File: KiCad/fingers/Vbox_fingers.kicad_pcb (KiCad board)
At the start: 2 copper layers, 109 x 45 mm, 20 parts, among them J1 Conn_01x10, J2 Conn_01x10, SW1 SW_Push_45deg, SW10 SW_Push_45deg, SW11 SW_Push_45deg, SW12 SW_Push_45deg, SW13 SW_Push_45deg, SW14 SW_Push_45deg, SW15 SW_Push_45deg, SW16 SW_Push_45deg, SW17 SW_Push_45deg, SW18 SW_Push_45deg, SW2 SW_Push_45deg, SW3 SW_Push_45deg, SW4 SW_Push_45deg, SW5 SW_Push_45deg, SW6 SW_Push_45deg, SW7 SW_Push_45deg, SW8 SW_Push_45deg, SW9 SW_Push_45deg

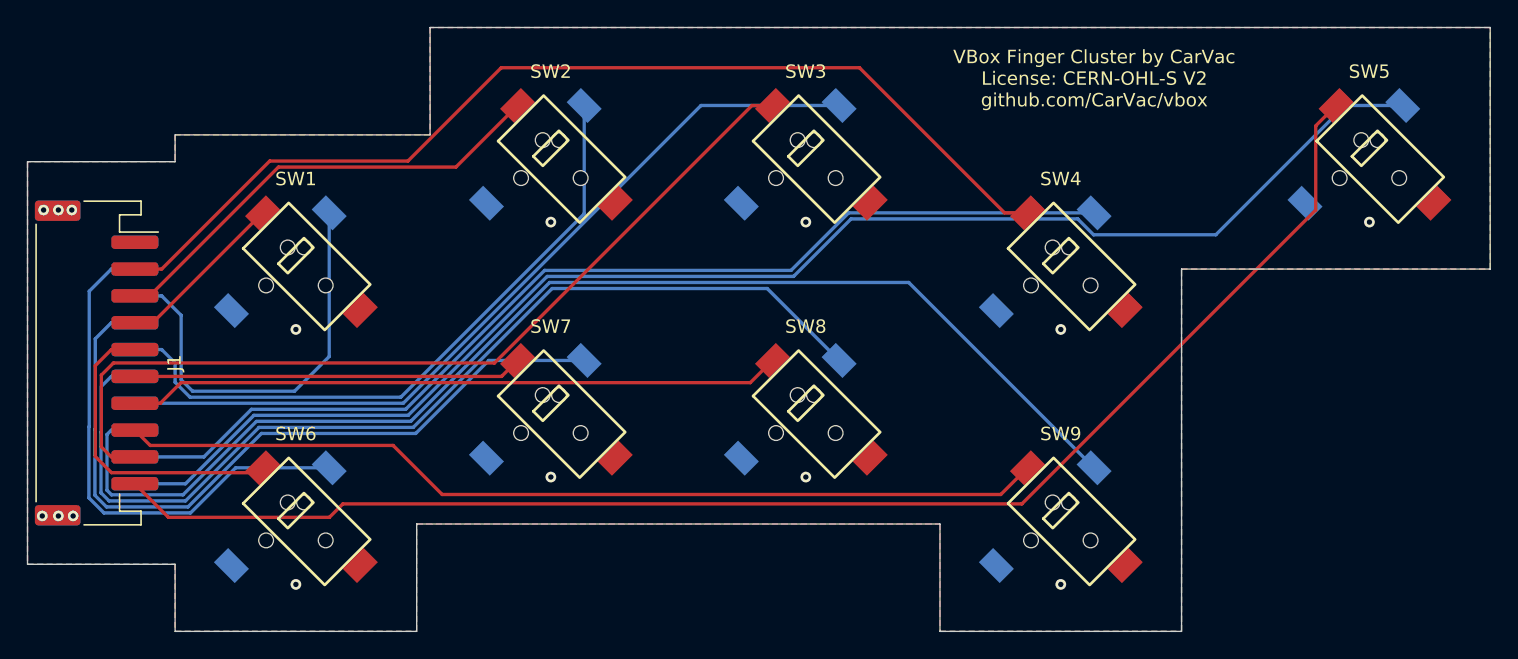
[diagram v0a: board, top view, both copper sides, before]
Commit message: tweak outlines of button clusters
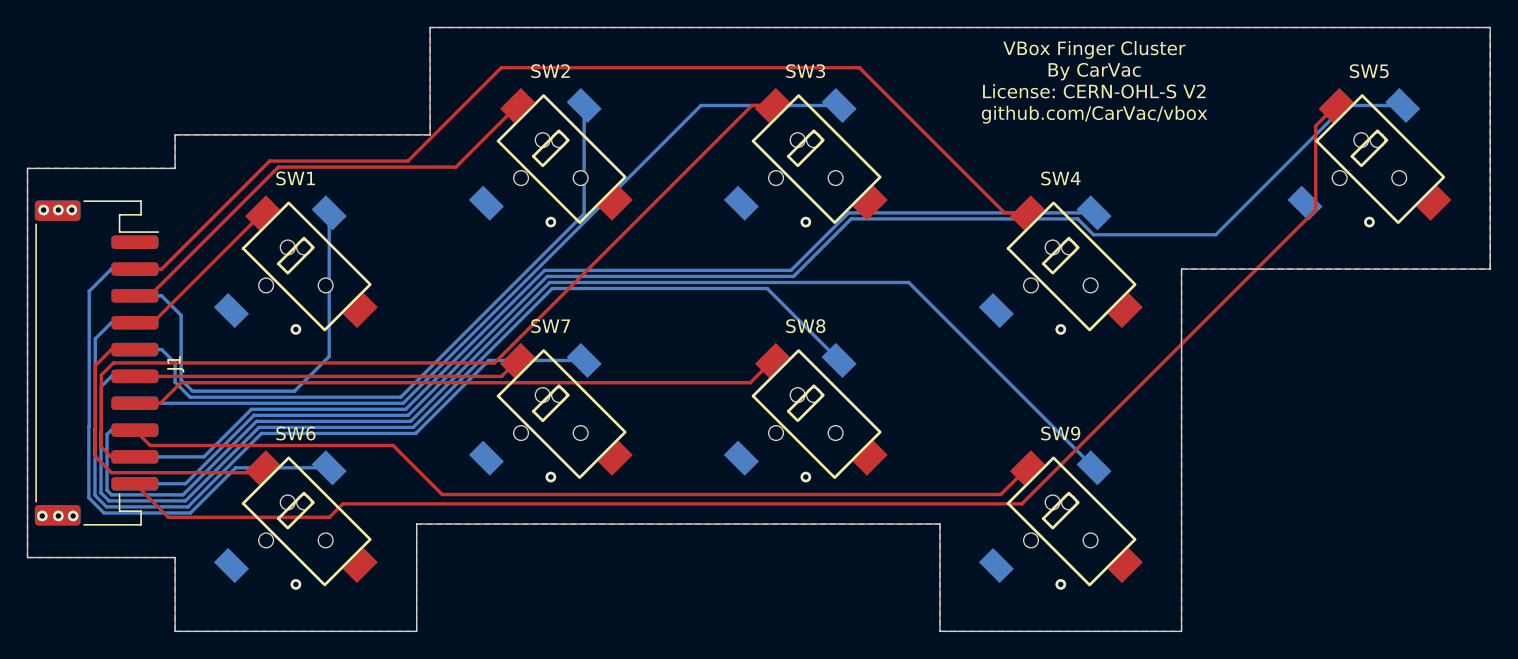
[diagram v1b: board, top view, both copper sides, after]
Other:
- outline, holes or cut-outs redrawn
- board text added: "VBox Finger Cluster By CarVac License: CERN-OHL-S V2 github.com/CarVac/vbox"
- board text removed: "VBox Finger Cluster by CarVac License: CERN-OHL-S V2 github.com/CarVac/vbox"
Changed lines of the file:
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@@
   (gr_poly
     (pts
-      (xy 91 123)
+      (xy 91 122.5)
       (xy 91 128)
       (xy 109 128)
@@
       (xy 110 91)
       (xy 91 91)
-      (xy 91 93)
-      (xy 80 93)
-      (xy 80 123)
+      (xy 91 93.5)
+      (xy 80 93.5)
+      (xy 80 122.5)
     )
     (stroke (width 0.1) (type solid)) (fill none) (layer "Edge.Cuts"))
-  (gr_text "VBox Finger Cluster by CarVac\nLicense: CERN-OHL-S V2\ngithub.com/CarVac/vbox" (at 159.5 89) (layer "F.SilkS")
+  (gr_text "VBox Finger Cluster\nBy CarVac\nLicense: CERN-OHL-S V2\ngithub.com/CarVac/vbox" (at 159.5 90) (layer "F.SilkS")
     (effects (font (size 1 1) (thickness 0.15)) (justify bottom))
   )
@@
     (polygon
       (pts
-        (xy 80 93)
-        (xy 80 123)
-        (xy 91 123)
+        (xy 80 93.5)
+        (xy 80 122.5)
+        (xy 91 122.5)
         (xy 91 128)
         (xy 109 128)
@@
         (xy 110 91)
         (xy 91 91)
-        (xy 91 93)
+        (xy 91 93.5)
       )
     )
@@
     (polygon
       (pts
-        (xy 80 93)
-        (xy 80 123)
-        (xy 91 123)
+        (xy 80 93.5)
+        (xy 80 122.5)
+        (xy 91 122.5)
         (xy 91 128)
         (xy 109 128)
@@
         (xy 110 91)
         (xy 91 91)
-        (xy 91 93)
+        (xy 91 93.5)
       )
     )

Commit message: fix drc errors
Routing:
- net MS: track 32.0 -> 33.6 mm
- net LS: track 49.5 -> 50.7 mm
- net INDEX2: track 77.2 -> 77.7 mm
- net GND: vias 15 -> 16

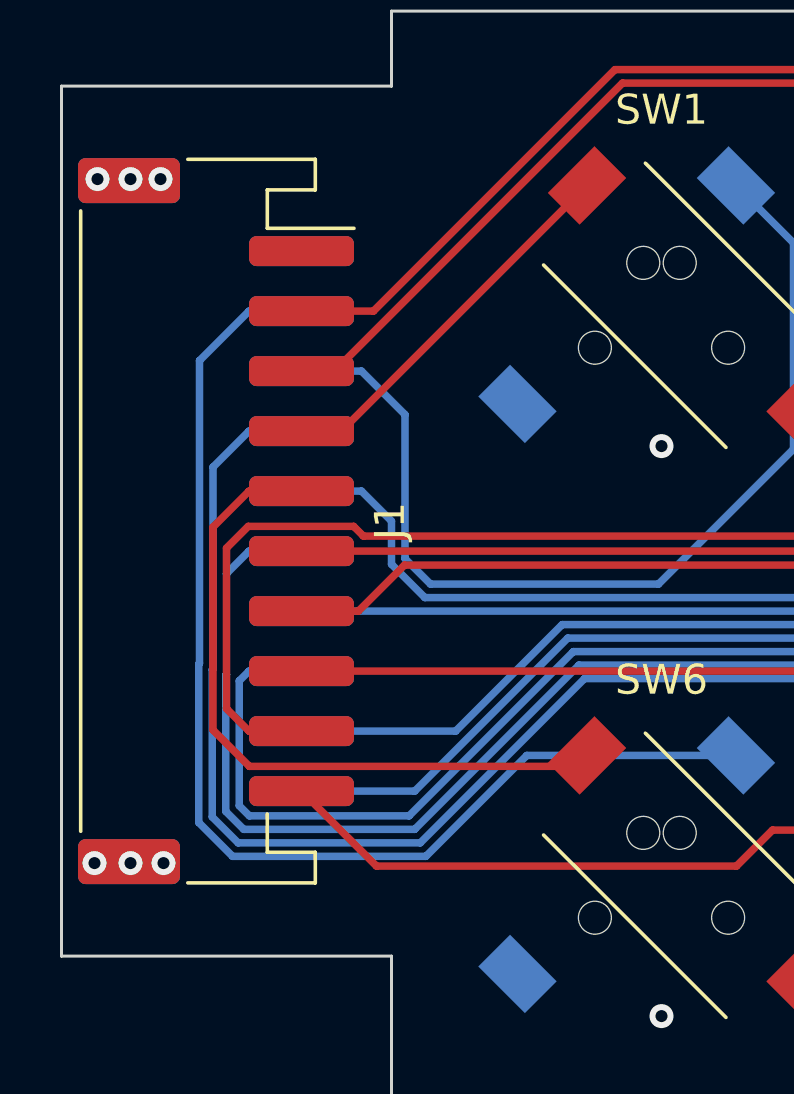
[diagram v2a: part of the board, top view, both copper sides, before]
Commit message: add thermal clearances to fingers, a few more vias
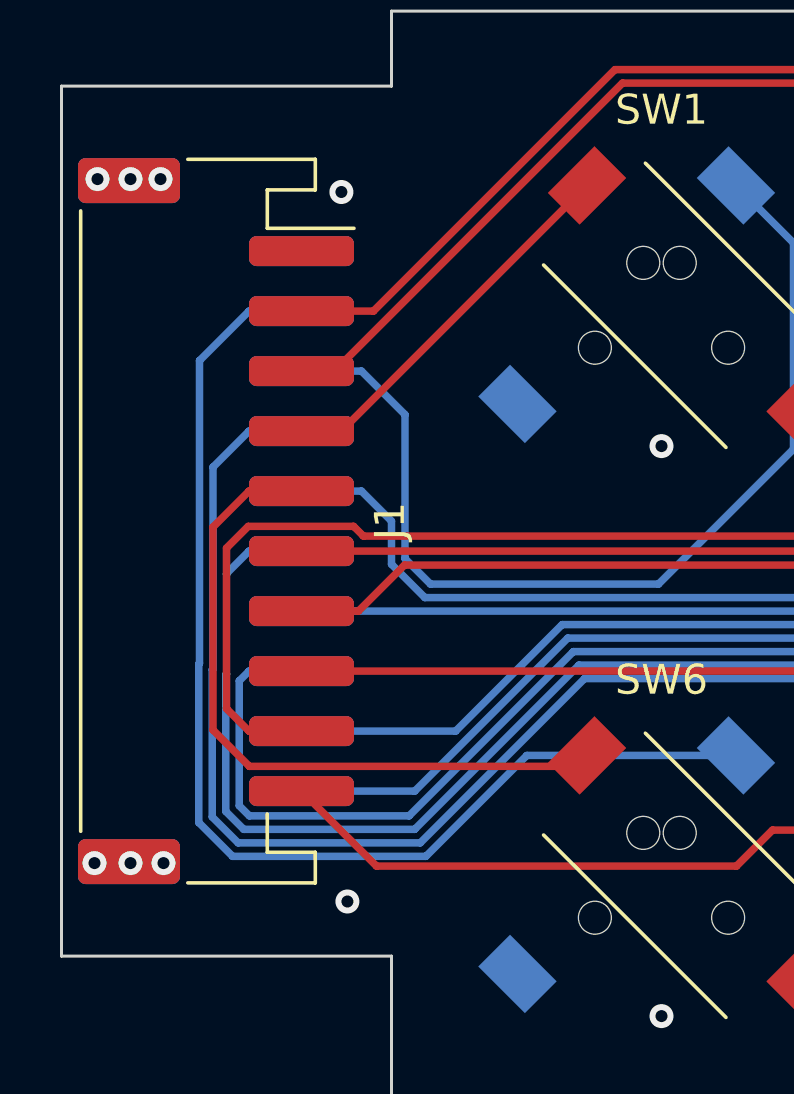
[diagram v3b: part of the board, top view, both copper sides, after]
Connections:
- SW1 pad 2: unconnected-(SW1-Pad2) -> GND
- SW10 pad 2: unconnected-(SW10-Pad2) -> GND
- SW11 pad 2: unconnected-(SW11-Pad2) -> GND
- SW12 pad 2: unconnected-(SW12-Pad2) -> GND
- SW13 pad 2: unconnected-(SW13-Pad2) -> GND
- SW14 pad 2: unconnected-(SW14-Pad2) -> GND
- SW15 pad 2: unconnected-(SW15-Pad2) -> GND
- SW16 pad 2: unconnected-(SW16-Pad2) -> GND
- SW17 pad 2: unconnected-(SW17-Pad2) -> GND
- SW18 pad 2: unconnected-(SW18-Pad2) -> GND
- SW2 pad 2: unconnected-(SW2-Pad2) -> GND
- SW3 pad 2: unconnected-(SW3-Pad2) -> GND
- SW4 pad 2: unconnected-(SW4-Pad2) -> GND
- SW5 pad 2: unconnected-(SW5-Pad2) -> GND
- SW6 pad 2: unconnected-(SW6-Pad2) -> GND
- SW7 pad 2: unconnected-(SW7-Pad2) -> GND
- SW8 pad 2: unconnected-(SW8-Pad2) -> GND
- SW9 pad 2: unconnected-(SW9-Pad2) -> GND
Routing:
- net GND: vias 16 -> 18

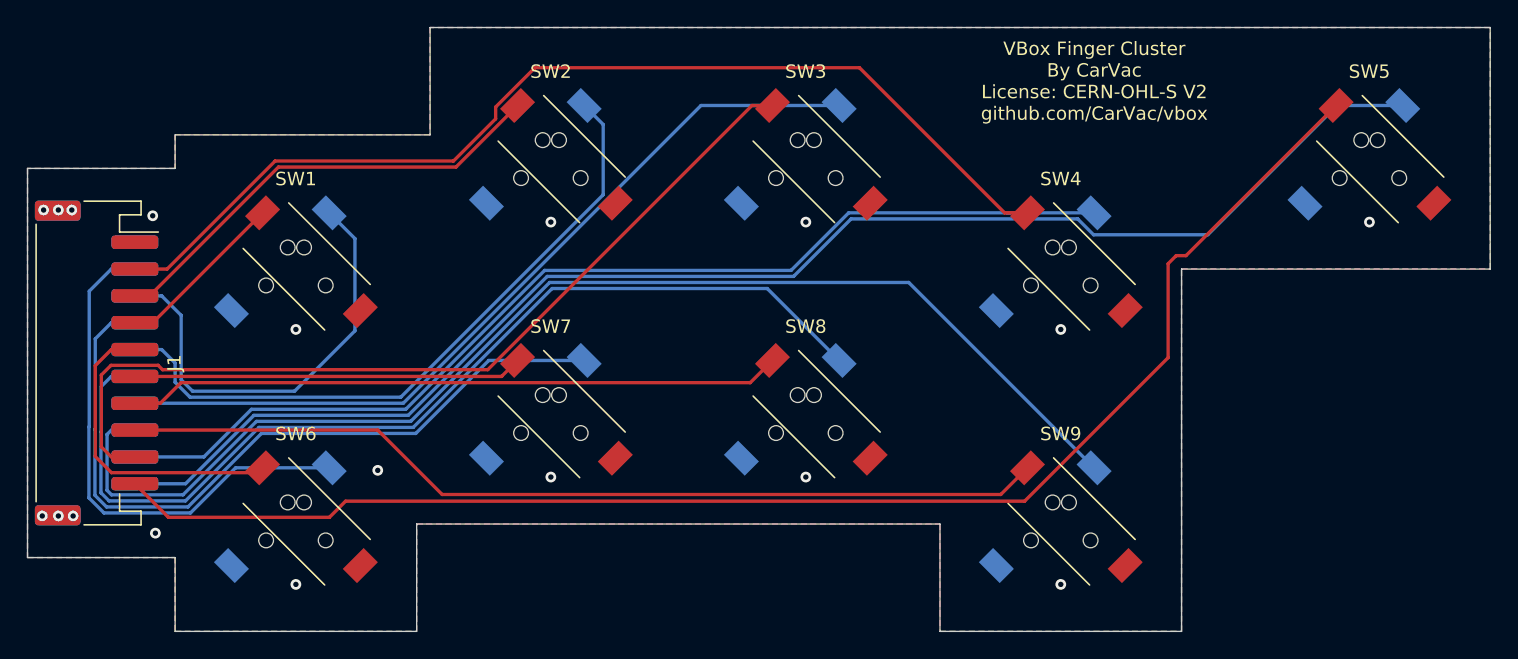
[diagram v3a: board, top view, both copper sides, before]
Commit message: rotate gnd connections for mouse switches
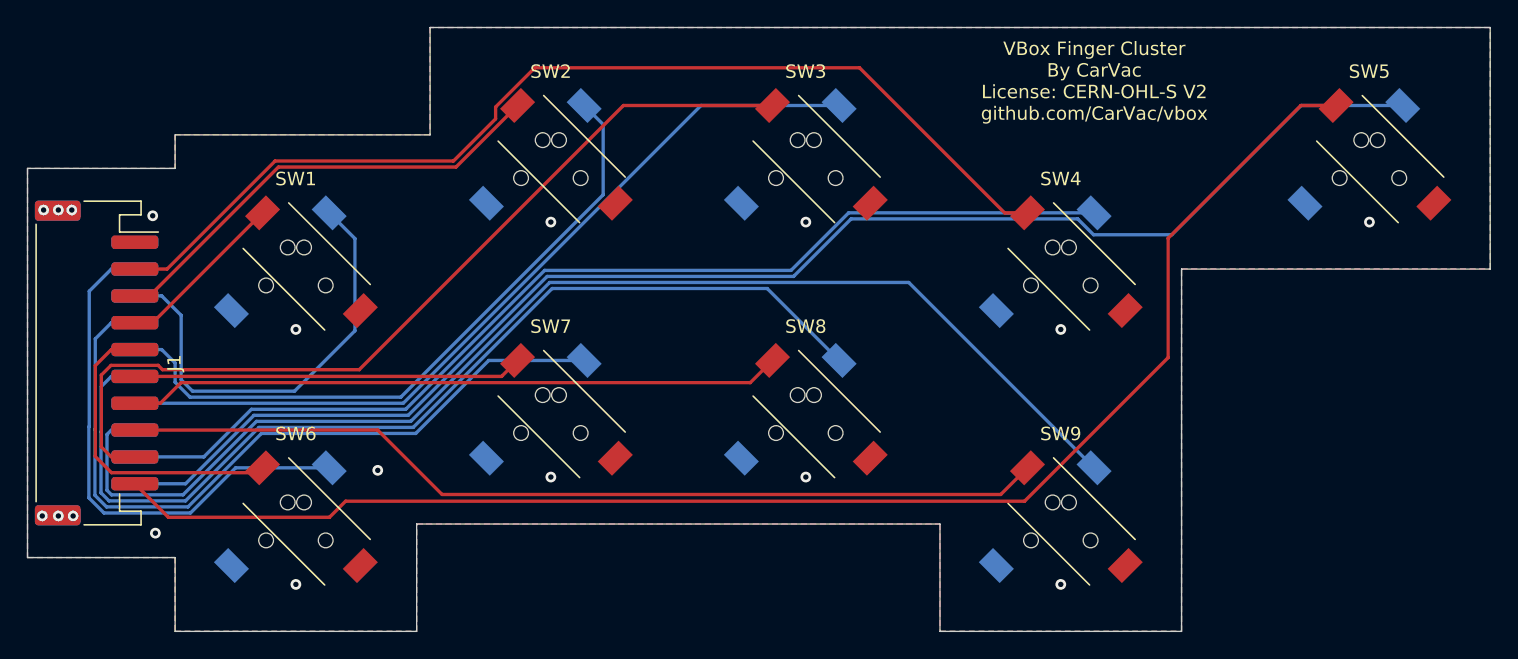
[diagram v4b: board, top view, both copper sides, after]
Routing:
- net START: track 107.4 -> 108.5 mm
